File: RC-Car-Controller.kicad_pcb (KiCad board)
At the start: 4 copper layers, 104 x 74 mm, 93 parts, among them J1 USB_C_Receptacle_USB2.0, J2 Power_Input, J3 Conn_01x11_Socket, J4 MOTOR_1_OUTPUT, J5 MOTOR_2_OUTPUT, J6 MOTOR_3_OUTPUT, J7 MOTOR_4_OUTPUT, J8 Conn_01x03_Socket, J9 Conn_01x11_Socket, SW2 SW_Push, SW4 SW_Push, U1 LMR14020SDDAR, U10 DRV8874PWPR, U11 DRV8874PWPR, U2 SPX3819M5-L-3-3, U3 USBLC6-2SC6, U4 BMI055, U5 DRV8874PWPR, U6 W25Q32JVSS, U8 ESP32-S3, U9 DRV8874PWPR, X2 40MHz

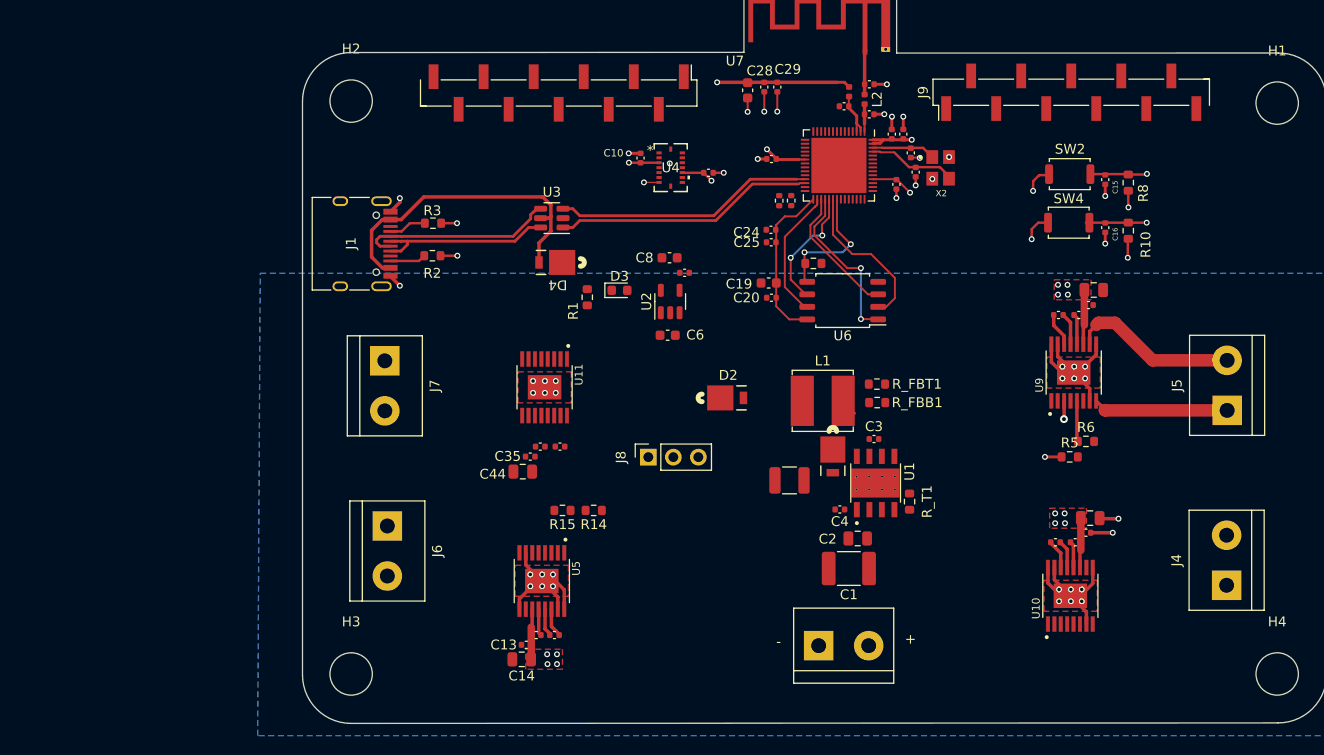
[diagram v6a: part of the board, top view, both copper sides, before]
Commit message: Add MPU6050 and LIS2MDL
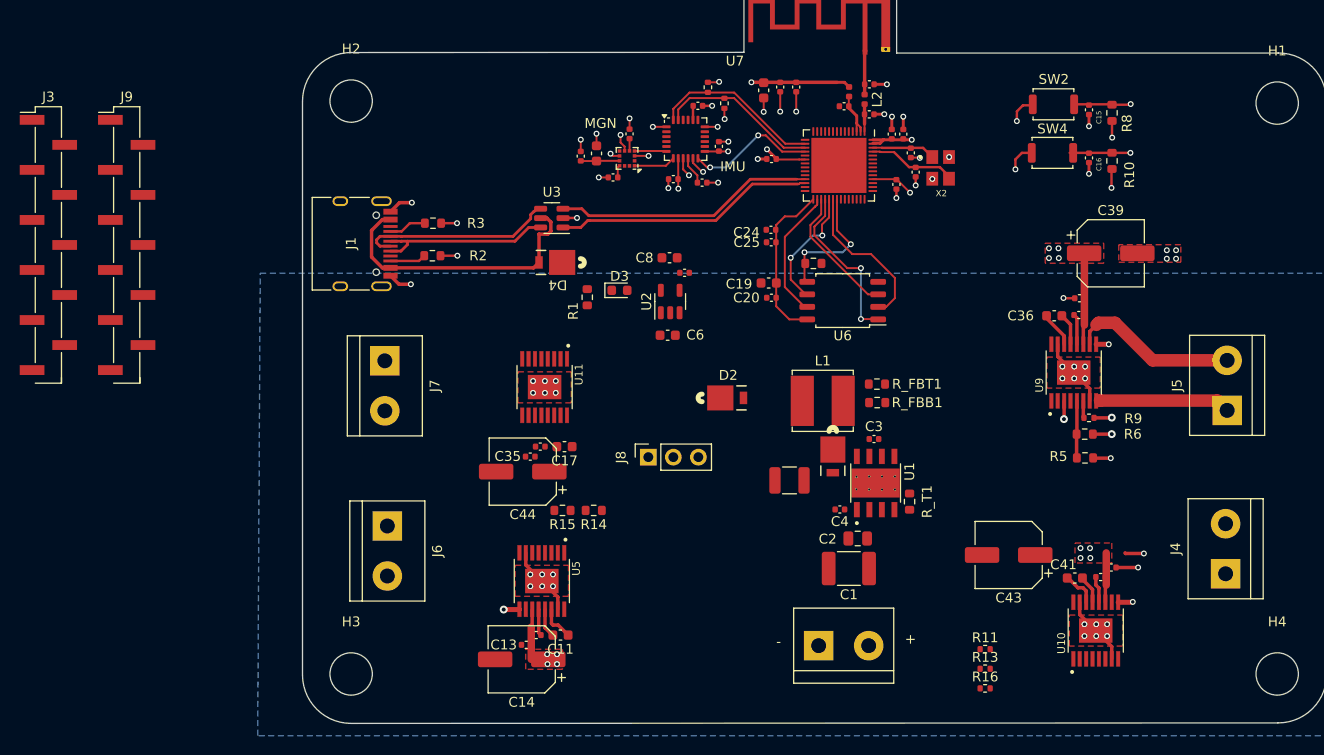
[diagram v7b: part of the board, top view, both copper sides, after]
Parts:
- removed C10, C9: 100n, Capacitor_SMD:C_0402_1005Metric
- removed R4, R7: 1k, Resistor_SMD:R_0402_1005Metric
- removed U4: BMI055, KiCADv6:LGA16_BMI055_BOS
- added C45: 100n, Capacitor_SMD:C_0402_1005Metric, F.Cu at (81.6, 42.6)
- added C46: 10u, Capacitor_SMD:C_0603_1608Metric, F.Cu at (79.9, 40.2)
- added C47: 100n, Capacitor_SMD:C_0402_1005Metric, F.Cu at (78.3, 40.4)
- added C48: 220n, Capacitor_SMD:C_0402_1005Metric, F.Cu at (83.3, 38.2)
- added C49: 100n, Capacitor_SMD:C_0402_1005Metric, F.Cu at (90.6, 43.1)
- added C50: 10n, Capacitor_SMD:C_0402_1005Metric, F.Cu at (87.7, 42.8)
- added C51: 100n, Capacitor_SMD:C_0402_1005Metric, F.Cu at (92.3, 39.4)
- added C52: 2n2, Capacitor_SMD:C_0402_1005Metric, F.Cu at (90.2, 35.3)
- added IMU: MPU-6050, Sensor_Motion:InvenSense_QFN-24_4x4mm_P0.5mm, F.Cu at (89.0, 38.7)
- added MGN: LIS2MDL, Package_LGA:LGA-12_2x2mm_P0.5mm, F.Cu at (83.0, 40.7)
- added R11: 1k, Resistor_SMD:R_0402_1005Metric, F.Cu at (119.4, 90.5)
- added R13: 1k, Resistor_SMD:R_0402_1005Metric, F.Cu at (119.4, 92.5)
- added R16: 1k, Resistor_SMD:R_0402_1005Metric, F.Cu at (119.4, 94.5)
- added R17: 1k, Resistor_SMD:R_0402_1005Metric, F.Cu at (91.2, 33.5)
- added R18: 1k, Resistor_SMD:R_0402_1005Metric, F.Cu at (92.9, 35.1)
- added R9: 1k, Resistor_SMD:R_0402_1005Metric, F.Cu at (129.9, 67.0)
- C11, C17, C36, C41: footprint Capacitor_SMD:C_0402_1005Metric -> Capacitor_SMD:C_0603_1608Metric
- C14, C39, C43, C44: footprint Capacitor_SMD:C_0805_2012Metric -> Capacitor_SMD:CP_Elec_6.3x7.7
- R14, R5: value 10K -> 16K
- R15, R6: value 10K -> 50K
- moved J9 97.1 mm to (32.2, 49.5), turned to 0 degrees
- moved J3 54.1 mm to (24.3, 49.5), turned to 0 degrees
- moved C43 9.09 mm to (121.7, 80.9), turned to 180 degrees
- moved C15 7.28 mm to (129.9, 35.7)
- moved C16 7.28 mm to (129.9, 40.6)
- moved SW2 7.28 mm to (126.3, 35.2)
- moved SW4 7.28 mm to (126.2, 40.1)
- moved R10 7.28 mm to (132.2, 40.9)
- moved R8 7.28 mm to (132.2, 36.0)
- moved C40 4.37 mm to (131.1, 83.2)
- moved C42 4.37 mm to (132.2, 82.2)
- moved U10 4.37 mm to (130.6, 88.6)
- moved C41 4.13 mm to (128.5, 83.3)
- moved C39 4.11 mm to (132.1, 50.3)
- moved C29 1.92 mm to (100.2, 33.4)
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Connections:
- net /Motors/MOTOR_VREF renamed /Motors/PROP_VREF
- U10 pad 16: GND -> MOTOR_1_PMODE
- U10 pad 17: GND -> (no net)
- U10 pad 4: unconnected-(U10-NFAULT-Pad4) -> MOTOR_1_NFAULT
- U10 pad 6: unconnected-(U10-IPROPI-Pad6) -> MOTOR_1_PROP
- U11 pad 16: GND -> MOTOR_4_PMODE
- U11 pad 17: GND -> (no net)
- U11 pad 4: unconnected-(U11-NFAULT-Pad4) -> MOTOR_4_NFAULT
- U11 pad 6: unconnected-(U11-IPROPI-Pad6) -> MOTOR_4_PROP
- U5 pad 16: GND -> MOTOR_3_PMODE
- U5 pad 17: GND -> (no net)
- U5 pad 4: unconnected-(U5-NFAULT-Pad4) -> MOTOR_3_NFAULT
- U5 pad 6: unconnected-(U5-IPROPI-Pad6) -> MOTOR_3_PROP
- U8 pad 12: GPIO7 -> MOTOR_4_PROP
- U8 pad 13: GPIO8 -> MOTOR_3_PROP
- U8 pad 14: GPIO9 -> MOTOR_2_PROP
- U8 pad 15: GPIO10 -> MOTOR_1_PROP
- U8 pad 16: GPIO11 -> SDA
- U8 pad 17: GPIO12 -> SCL
- U8 pad 18: GPIO13 -> INT_IMU
- U8 pad 23: INT_GYR_1 -> GPIO17
- U8 pad 24: INT_ACC_1 -> GPIO18
- U8 pad 27: SDA -> unconnected-(U8-GPIO21-Pad27)
- U8 pad 28: SCL -> unconnected-(U8-SPI_CS1/GPIO26-Pad28)
- U8 pad 51: ADDR_GYRO -> unconnected-(U8-GPIO45-Pad51)
- U8 pad 52: ADDR_ACCEL -> unconnected-(U8-GPIO46-Pad52)
- U9 pad 16: GND -> MOTOR_2_PMODE
- U9 pad 17: GND -> (no net)
- U9 pad 4: unconnected-(U9-NFAULT-Pad4) -> MOTOR_2_NFAULT
- U9 pad 6: unconnected-(U9-IPROPI-Pad6) -> MOTOR_2_PROP
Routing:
- net SDA: track 0.00 -> 17.3 mm
- net SCL: track 0.00 -> 16.5 mm
- net INT_IMU: track 0.00 -> 13.3 mm, vias 0 -> 2
- net /Sensors/MGN_SCL: track 0.00 -> 4.24 mm
- net +36V: track 15.7 -> 19.4 mm
- net +VBUS: track 32.5 -> 29.1 mm
- net /Sensors/MGN_SDA: track 0.00 -> 3.25 mm
- net Net-(U13-REGOUT): track 0.00 -> 2.86 mm
- net GND: track 82.1 -> 84.8 mm, vias 50 -> 72
- net +3V3: track 42.6 -> 44.5 mm, vias 11 -> 13
- net MOTOR_2_PROP: track 0.00 -> 1.75 mm
- net /Motors/PROP_VREF: track 4.15 -> 5.91 mm
- net Net-(U13-CPOUT): track 0.00 -> 1.43 mm
- net /Sensors/VDD_IO: track 0.00 -> 1.26 mm
- net Net-(U12-C1): track 0.00 -> 1.24 mm
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
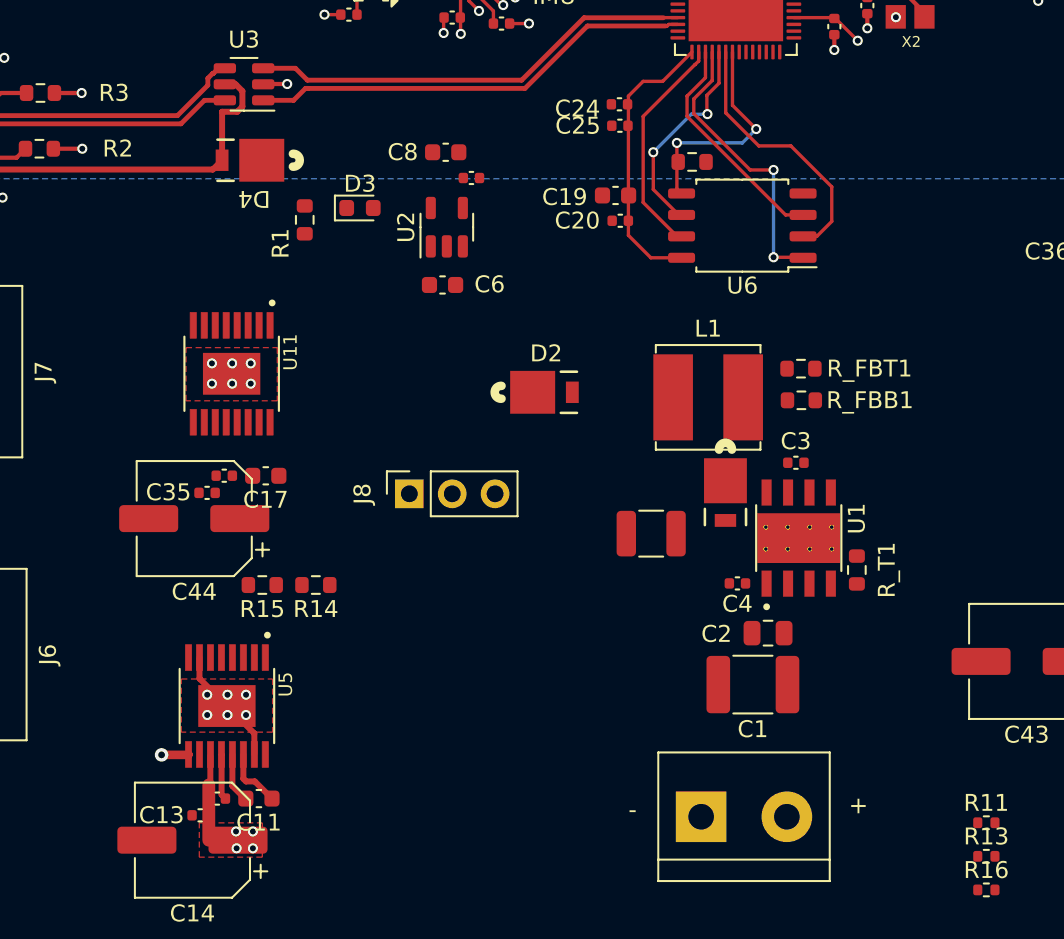
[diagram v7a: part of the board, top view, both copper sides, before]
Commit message: modify layout
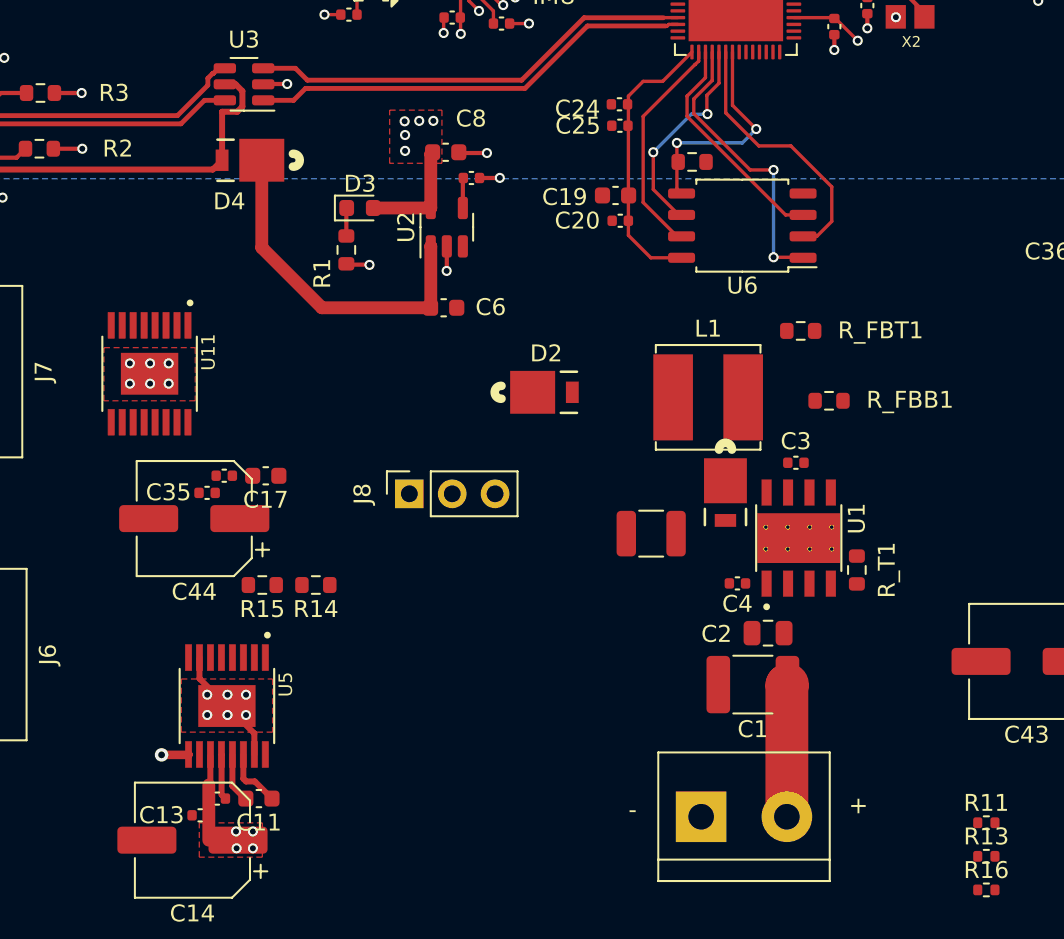
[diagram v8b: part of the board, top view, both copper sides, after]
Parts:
- moved U11 4.86 mm to (69.8, 63.9)
- moved R1 3.04 mm to (81.4, 56.5)
- moved R_FBT1 2.24 mm to (108.4, 61.3)
- moved R_FBB1 1.64 mm to (110.0, 65.5), turned to 0 degrees
- moved C6 1.35 mm to (87.2, 60.0)
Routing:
- net +5V: track 0.00 -> 20.3 mm
- net +36V: track 19.4 -> 27.3 mm
- net +3V3: track 44.5 -> 51.2 mm, vias 13 -> 18
- net GND: track 84.8 -> 90.5 mm, vias 72 -> 76
- net Net-(U2-BP): track 0.00 -> 1.79 mm
- net Net-(D3-K): track 0.00 -> 1.67 mm
- added copper zone on F.Cu, net +3V3
